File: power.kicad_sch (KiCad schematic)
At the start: 71 parts, among them J1 Barrel_Jack

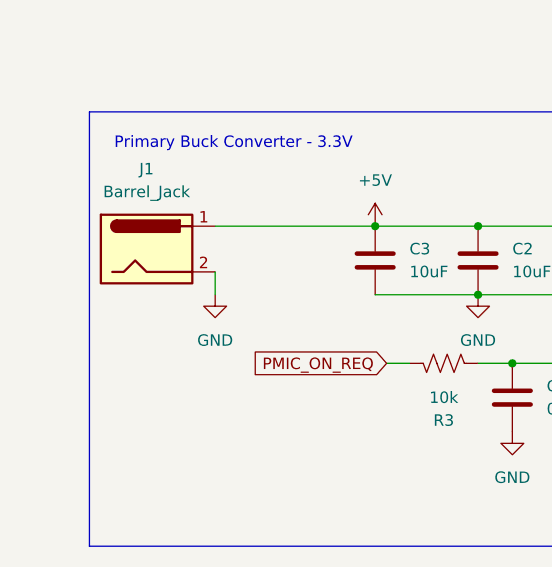
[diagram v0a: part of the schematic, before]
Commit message: Add in LCSC part numbers for major parts, assign packages
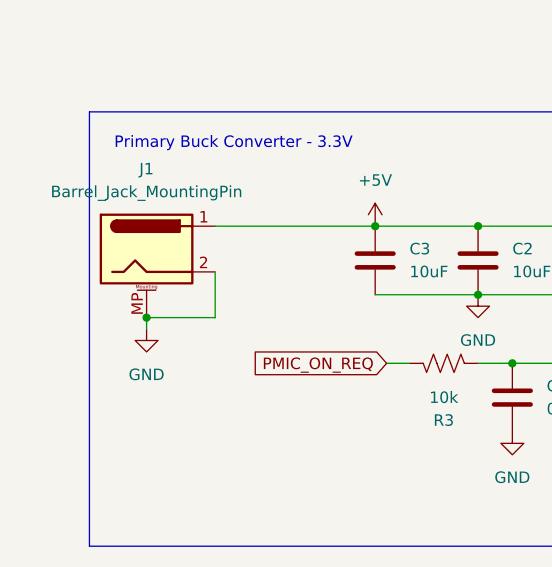
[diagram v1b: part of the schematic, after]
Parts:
- removed J1: Barrel_Jack, symbol Connector:Barrel_Jack
- added J1: Barrel_Jack_MountingPin, Connector_BarrelJack:BarrelJack_CUI_PJ-063AH_Horizontal, symbol Connector:Barrel_Jack_MountingPin
- BT1: LCSC Part # (none) -> C18212226
- C1, C11, C12, C14, C15, C17, C19, C20, C22, C23, C24, C26, C28, C29, C31, C32, C33, C34, C35, C37, C38, C39, C4, C5, C8: footprint (none) -> Capacitor_SMD:C_0402_1005Metric
- C10, C13, C16, C18, C2, C21, C25, C27, C3, C30, C36, C6, C7, C9: footprint (none) -> Capacitor_SMD:C_0603_1608Metric
- Q1: LCSC Part # (none) -> C509962
- Q2, Q3: LCSC Part # (none) -> C113315
- R1, R10, R11, R12, R13, R14, R15, R16, R17, R2, R3, R4, R5, R6, R7, R8, R9: footprint (none) -> Resistor_SMD:R_0402_1005Metric
- U1: LCSC Part # (none) -> C414042
- U2: LCSC Part # (none) -> C3193214
- U3, U4: LCSC Part # (none) -> C3194257
- U5: LCSC Part # (none) -> C620011
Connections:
- net +5V: now also J1.1
- net GND: now also J1.2, J1.MP (MountPin)
